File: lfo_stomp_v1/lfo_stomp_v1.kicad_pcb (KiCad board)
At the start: 2 copper layers, 33.5 x 100 mm, 50 parts, among them J1 Conn_02x05_Odd_Even, J2 SYNC_IN, J3 LFO_INV, J4 LFO, Q1 BC547, Q2 2N3906, SW1 SW_Push, U1 LM7805_TO220, U2 ElectricDruid_STOMPLFO, U3 TL072, U4 L78L05_SOT89

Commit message: Geographic reannotate
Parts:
- renumbered C11 to C10, C9 to C100, C8 to C101, C7 to C11, C10 to C12, C3 to C2, C6 to C3, C1 to C4, C4 to C5, C13 to C6, C5 to C7, C12 to C8, C2 to C9, D4 to D100, D1 to D2, D2 to D3, D3 to D4, FB2 to FB1, FB1 to FB2, J2 to J100, J4 to J101, J3 to J102, J1 to J2, LOGO1 to LOGO100, LOGO2 to LOGO101, LOGO3 to LOGO2, R8 to R10, R9 to R12, R10 to R13, R3 to R2, R2 to R3, R13 to R5, R7 to R6, R5 to R7, R6 to R8, R12 to R9, R_DEPTH1 to R_DEPTH100, R_FREQ1 to R_FREQ100, R_OFFSET1 to R_OFFSET100, R_WAVEFORM1 to R_WAVEFORM100, SW1 to SW100, U4 to U2, U2 to U4

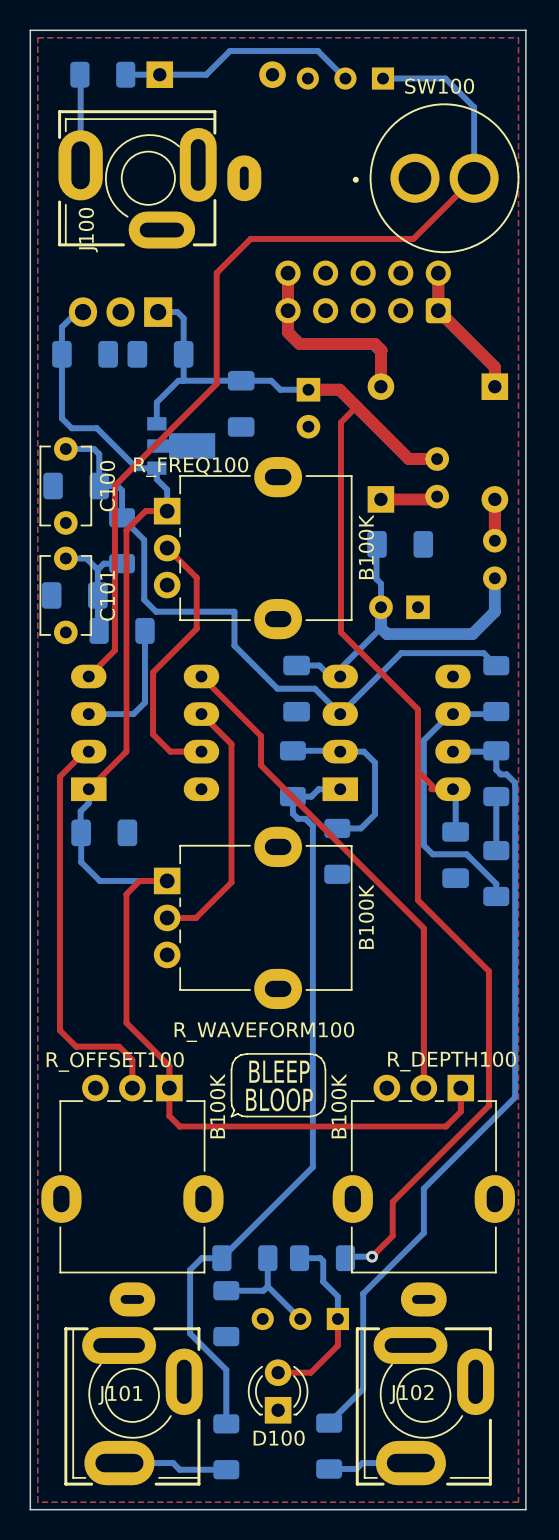
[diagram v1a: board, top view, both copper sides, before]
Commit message: Page titles and fixed pot orientations
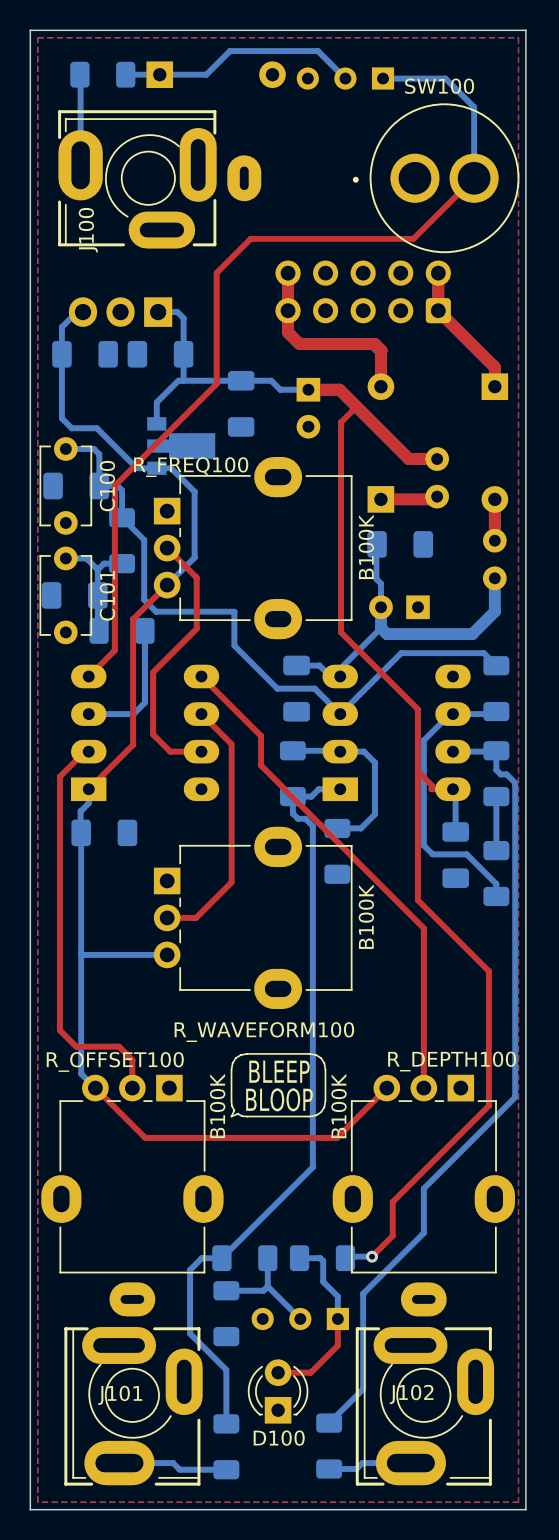
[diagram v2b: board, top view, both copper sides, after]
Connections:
- R_DEPTH100 pad 1: +5V -> GND
- R_DEPTH100 pad 3: GND -> +5V
- R_FREQ100 pad 1: +5V -> GND
- R_FREQ100 pad 3: GND -> +5V
- R_OFFSET100 pad 1: +5V -> GND
- R_OFFSET100 pad 3: GND -> +5V
- R_WAVEFORM100 pad 1: +5V -> GND
- R_WAVEFORM100 pad 3: GND -> +5V
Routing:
- net +5V: track 93.7 -> 91.3 mm
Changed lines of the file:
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@@
   )
   (paper "A4")
+  (title_block
+    (title "STOMPLFO")
+    (date "2022-06-25")
+    (rev "1.0")
+    (company "RobotDialogs")
+  )
   (layers
     (0 "F.Cu" signal)
@@
     (fp_circle (center 0 0) (end 0 -3.5) (layer "F.Fab") (width 0.1) (fill none))
     (pad "1" thru_hole rect (at -7.5 -2.5 90) (size 1.8 1.8) (drill 1) (layers *.Cu *.Mask)
-      (net 4 "+5V") (pinfunction "1") (pintype "passive"))
+      (net 2 "GND") (pinfunction "1") (pintype "passive"))
     (pad "2" thru_hole circle (at -7.5 0 90) (size 1.8 1.8) (drill 1) (layers *.Cu *.Mask)
       (net 28 "Net-(U4-Pad7)") (pinfunction "2") (pintype "passive"))
     (pad "3" thru_hole circle (at -7.5 2.5 90) (size 1.8 1.8) (drill 1) (layers *.Cu *.Mask)
-      (net 2 "GND") (pinfunction "3") (pintype "passive"))
+      (net 4 "+5V") (pinfunction "3") (pintype "passive"))
     (pad "MP" thru_hole oval (at 0 4.8 90) (size 2.72 3.24) (drill oval 1.1 1.8) (layers *.Cu *.Mask)
       (net 2 "GND") (pinfunction "MountPin") (pintype "passive"))
@@
     (fp_circle (center 0 0) (end 0 -3.5) (layer "F.Fab") (width 0.1) (fill none))
     (pad "1" thru_hole rect (at -7.5 -2.5) (size 1.8 1.8) (drill 1) (layers *.Cu *.Mask)
-      (net 4 "+5V") (pinfunction "1") (pintype "passive"))
+      (net 2 "GND") (pinfunction "1") (pintype "passive"))
     (pad "2" thru_hole circle (at -7.5 0) (size 1.8 1.8) (drill 1) (layers *.Cu *.Mask)
       (net 27 "Net-(U4-Pad5)") (pinfunction "2") (pintype "passive"))
     (pad "3" thru_hole circle (at -7.5 2.5) (size 1.8 1.8) (drill 1) (layers *.Cu *.Mask)
-      (net 2 "GND") (pinfunction "3") (pintype "passive"))
+      (net 4 "+5V") (pinfunction "3") (pintype "passive"))
     (pad "MP" thru_hole oval (at 0 -4.8) (size 2.72 3.24) (drill oval 1.1 1.8) (layers *.Cu *.Mask)
       (net 2 "GND") (pinfunction "MountPin") (pintype "passive"))
@@
     (fp_circle (center 0 0) (end 0 -3.5) (layer "F.Fab") (width 0.1) (fill none))
     (pad "1" thru_hole rect (at -7.5 -2.5 90) (size 1.8 1.8) (drill 1) (layers *.Cu *.Mask)
-      (net 4 "+5V") (pinfunction "1") (pintype "passive"))
+      (net 2 "GND") (pinfunction "1") (pintype "passive"))
     (pad "2" thru_hole circle (at -7.5 0 90) (size 1.8 1.8) (drill 1) (layers *.Cu *.Mask)
       (net 30 "Net-(U4-Pad6)") (pinfunction "2") (pintype "passive"))
     (pad "3" thru_hole circle (at -7.5 2.5 90) (size 1.8 1.8) (drill 1) (layers *.Cu *.Mask)
-      (net 2 "GND") (pinfunction "3") (pintype "passive"))
+      (net 4 "+5V") (pinfunction "3") (pintype "passive"))
     (pad "MP" thru_hole oval (at 0 -4.8 90) (size 2.72 3.24) (drill oval 1.1 1.8) (layers *.Cu *.Mask)
       (net 2 "GND") (pinfunction "MountPin") (pintype "passive"))
@@
     (fp_circle (center 0 0) (end 0 -3.5) (layer "F.Fab") (width 0.1) (fill none))
     (pad "1" thru_hole rect (at -7.5 -2.5) (size 1.8 1.8) (drill 1) (layers *.Cu *.Mask)
-      (net 4 "+5V") (pinfunction "1") (pintype "passive"))
+      (net 2 "GND") (pinfunction "1") (pintype "passive"))
     (pad "2" thru_hole circle (at -7.5 0) (size 1.8 1.8) (drill 1) (layers *.Cu *.Mask)
       (net 29 "Net-(U4-Pad2)") (pinfunction "2") (pintype "passive"))
     (pad "3" thru_hole circle (at -7.5 2.5) (size 1.8 1.8) (drill 1) (layers *.Cu *.Mask)
-      (net 2 "GND") (pinfunction "3") (pintype "passive"))
+      (net 4 "+5V") (pinfunction "3") (pintype "passive"))
     (pad "MP" thru_hole oval (at 0 -4.8) (size 2.72 3.24) (drill oval 1.1 1.8) (layers *.Cu *.Mask)
       (net 2 "GND") (pinfunction "MountPin") (pintype "passive"))
@@
   (segment (start 160.28 93.68) (end 159.5375 92.9375) (width 0.4) (layer "B.Cu") (net 3))
   (segment (start 163.705113 89) (end 163.705113 90.405113) (width 0.8) (layer "B.Cu") (net 3))
-  (segment (start 146.5 117.1) (end 149.4 120) (width 0.4) (layer "F.Cu") (net 4))
-  (segment (start 149.25 82.5) (end 147.8 82.5) (width 0.4) (layer "F.Cu") (net 4))
-  (segment (start 147.8 82.5) (end 146.5 83.8) (width 0.4) (layer "F.Cu") (net 4))
-  (segment (start 146.5 98.75) (end 143.95 101.3) (width 0.4) (layer "F.Cu") (net 4))
-  (segment (start 146.5 83.8) (end 146.5 98.75) (width 0.4) (layer "F.Cu") (net 4))
-  (segment (start 168.1 124.1) (end 150.1 124.1) (width 0.4) (layer "F.Cu") (net 4))
-  (segment (start 149.25 107.5) (end 147.4 107.5) (width 0.4) (layer "F.Cu") (net 4))
-  (segment (start 150.1 124.1) (end 149.4 123.4) (width 0.4) (layer "F.Cu") (net 4))
-  (segment (start 169.1 121.5) (end 169.1 123.1) (width 0.4) (layer "F.Cu") (net 4))
-  (segment (start 149.4 120) (end 149.4 121.5) (width 0.4) (layer "F.Cu") (net 4))
-  (segment (start 146.5 108.4) (end 146.5 117.1) (width 0.4) (layer "F.Cu") (net 4))
-  (segment (start 169.1 123.1) (end 168.1 124.1) (width 0.4) (layer "F.Cu") (net 4))
-  (segment (start 147.4 107.5) (end 146.5 108.4) (width 0.4) (layer "F.Cu") (net 4))
-  (segment (start 149.4 123.4) (end 149.4 121.5) (width 0.4) (layer "F.Cu") (net 4))
+  (segment (start 146.95 89.8) (end 146.95 98.3) (width 0.4) (layer "F.Cu") (net 4))
+  (segment (start 160.73 124.87) (end 164.1 121.5) (width 0.4) (layer "F.Cu") (net 4))
+  (segment (start 144.4 121.5) (end 147.77 124.87) (width 0.4) (layer "F.Cu") (net 4))
+  (segment (start 146.95 98.3) (end 143.95 101.3) (width 0.4) (layer "F.Cu") (net 4))
+  (segment (start 149.25 87.5) (end 146.95 89.8) (width 0.4) (layer "F.Cu") (net 4))
+  (segment (start 147.77 124.87) (end 160.73 124.87) (width 0.4) (layer "F.Cu") (net 4))
   (segment (start 142.8 76.9) (end 144.5 76.9) (width 0.4) (layer "B.Cu") (net 4))
+  (segment (start 151.11 81.19) (end 149.52 79.6) (width 0.4) (layer "B.Cu") (net 4))
   (segment (start 143.56 69.045) (end 143.155 69.045) (width 0.4) (layer "B.Cu") (net 4))
-  (segment (start 143.4375 106.2375) (end 143.4375 104.25) (width 0.4) (layer "B.Cu") (net 4))
   (segment (start 142.1375 76.2375) (end 142.8 76.9) (width 0.4) (layer "B.Cu") (net 4))
+  (segment (start 143.4375 112.3975) (end 143.4375 120.5375) (width 0.4) (layer "B.Cu") (net 4))
+  (segment (start 143.4375 120.5375) (end 144.4 121.5) (width 0.4) (layer "B.Cu") (net 4))
   (segment (start 147.2 79.6) (end 148.55 79.6) (width 0.4) (layer "B.Cu") (net 4))
-  (segment (start 149.25 82.5) (end 149.25 81.05) (width 0.4) (layer "B.Cu") (net 4))
-  (segment (start 144.7 107.5) (end 143.4375 106.2375) (width 0.4) (layer "B.Cu") (net 4))
+  (segment (start 149.25 87.5) (end 151.11 85.64) (width 0.4) (layer "B.Cu") (net 4))
+  (segment (start 143.4375 104.25) (end 143.4375 112.3975) (width 0.4) (layer "B.Cu") (net 4))
   (segment (start 142.1375 70.0625) (end 142.1375 71.9) (width 0.4) (layer "B.Cu") (net 4))
-  (segment (start 149.25 81.05) (end 148.55 80.35) (width 0.4) (layer "B.Cu") (net 4))
   (segment (start 143.4 104.2125) (end 143.4375 104.25) (width 0.4) (layer "B.Cu") (net 4))
-  (segment (start 148.55 80.35) (end 148.55 79.6) (width 0.4) (layer "B.Cu") (net 4))
   (segment (start 143.95 101.3) (end 143.95 102.25) (width 0.4) (layer "B.Cu") (net 4))
+  (segment (start 143.54 112.5) (end 143.4375 112.3975) (width 0.4) (layer "B.Cu") (net 4))
   (segment (start 142.1375 71.9) (end 142.1375 76.2375) (width 0.4) (layer "B.Cu") (net 4))
+  (segment (start 149.25 112.5) (end 143.54 112.5) (width 0.4) (layer "B.Cu") (net 4))
   (segment (start 144.5 76.9) (end 147.2 79.6) (width 0.4) (layer "B.Cu") (net 4))
-  (segment (start 149.25 107.5) (end 144.7 107.5) (width 0.4) (layer "B.Cu") (net 4))
+  (segment (start 149.52 79.6) (end 148.55 79.6) (width 0.4) (layer "B.Cu") (net 4))
   (segment (start 143.4 102.8) (end 143.4 104.2125) (width 0.4) (layer "B.Cu") (net 4))
   (segment (start 143.95 102.25) (end 143.4 102.8) (width 0.4) (layer "B.Cu") (net 4))
   (segment (start 143.155 69.045) (end 142.1375 70.0625) (width 0.4) (layer "B.Cu") (net 4))
+  (segment (start 151.11 85.64) (end 151.11 81.19) (width 0.4) (layer "B.Cu") (net 4))
   (segment (start 171.4 74.09) (end 171.4 72.7725) (width 0.8) (layer "F.Cu") (net 5))
   (segment (start 171.4 72.7725) (end 167.58 68.9525) (width 0.8) (layer "F.Cu") (net 5))

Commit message: Cleanup
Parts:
- D100: value LED? -> LED
- Q2: value 2N3906 -> BC547
- R1: value 100k -> 10k
- R10: value 100k -> 2k
- R11: value 22k -> 10k
- R9: value 3.3k -> 10k
- moved R12 15.5 mm to (170.9, 134.5)
- moved R13 2.38 mm to (155.2, 147.2), turned to 180 degrees
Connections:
- D100 pad 1: GND -> Net-(D100-Pad1)
- D100 pad 2: Net-(D100-Pad2) -> +12V
- Q2 pad 1: Net-(D100-Pad2) -> Net-(R9-Pad2)
- R10 pad 2: Net-(R13-Pad1) -> Net-(R3-Pad1)
- R9 pad 1: +12V -> Net-(D100-Pad1)
- R9 pad 2: Net-(D100-Pad2) -> Net-(R9-Pad2)
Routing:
- net Net-(R3-Pad1): track 8.97 -> 49.1 mm
- net Net-(D100-Pad1): track 0.00 -> 20.2 mm, vias 0 -> 1
- net Net-(D100-Pad2): track 12.6 -> 0.00 mm
- net Net-(R12-Pad1): track 54.4 -> 41.8 mm
- net Net-(R13-Pad1): track 51.9 -> 63.8 mm
- net Net-(J102-PadT): track 5.69 -> 16.8 mm
- net +12V: track 113.5 -> 122.8 mm, vias 1 -> 0
- net Net-(R9-Pad2): track 0.00 -> 5.98 mm
- net Net-(R6-Pad1): track 12.3 -> 14.2 mm
- net Net-(R10-Pad1): track 7.94 -> 8.84 mm
